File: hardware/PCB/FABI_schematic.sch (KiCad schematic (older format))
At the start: 40 parts, among them J1 Cliff_68125, J10 Conn_01x03_Male, J11 dispaly_connector_91601-304LF, J2 Cliff_68125, J3 Cliff_68125, J4 Cliff_68125, J5 Cliff_68125, J6 Cliff_68125, J7 Cliff_68125, J8 Cliff_68125, J9 Conn_02x05_Odd_Even, U1 MPXV7007GP, U2 ProMicro

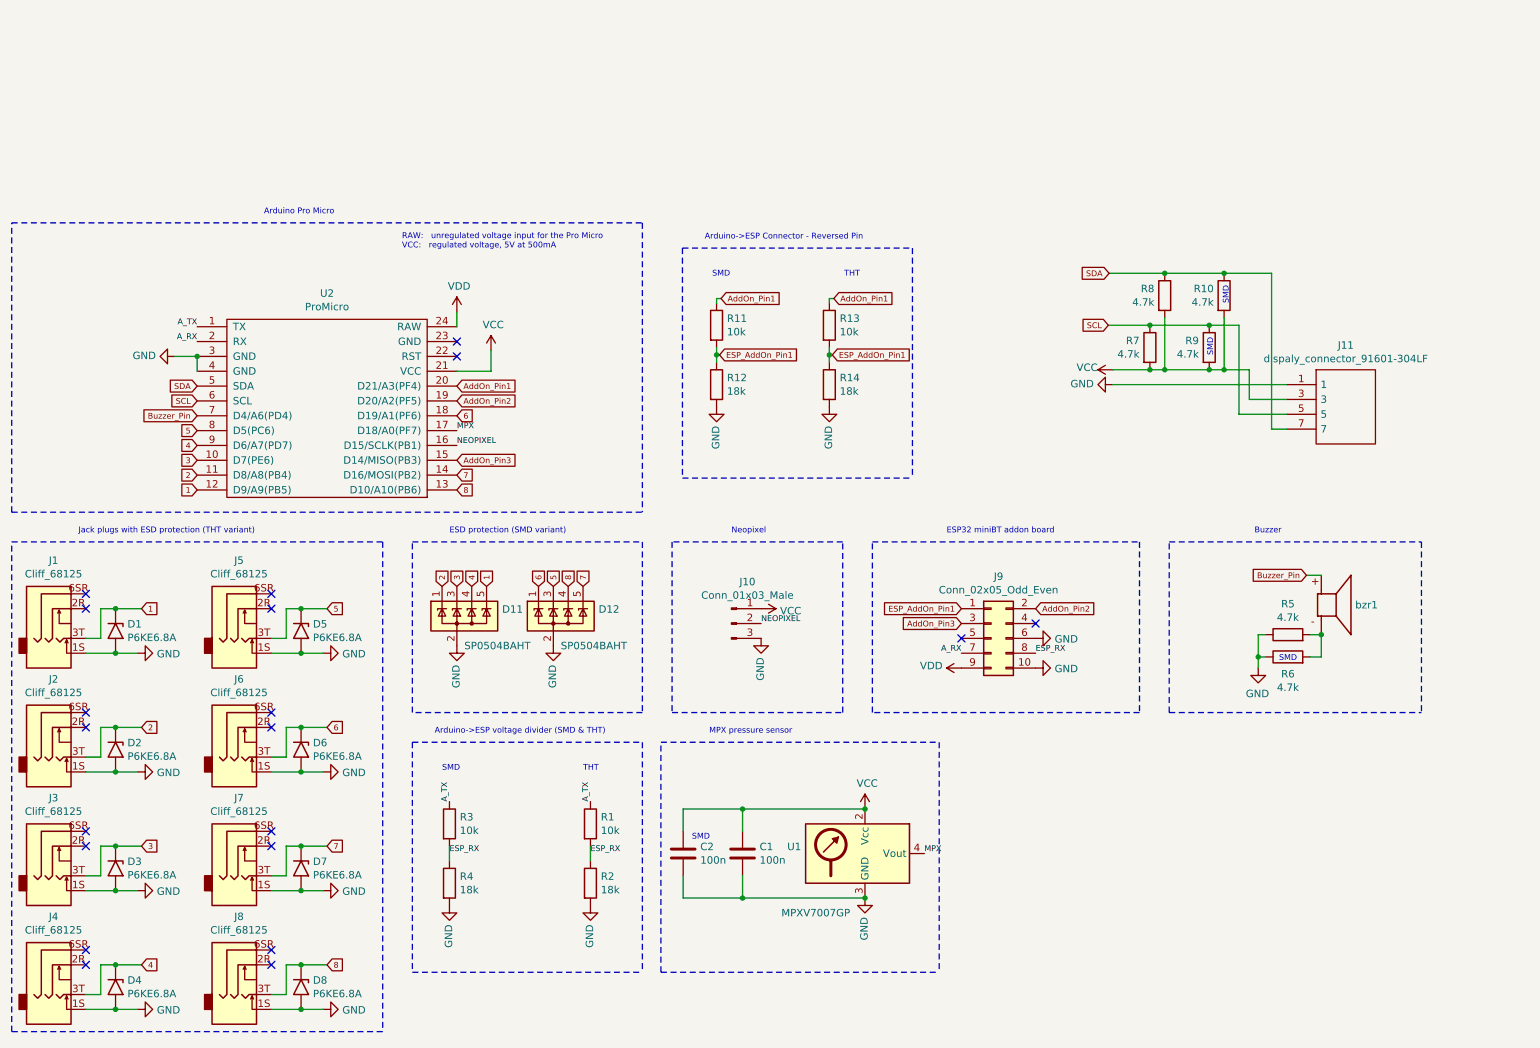
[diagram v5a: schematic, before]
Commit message: PCB v2, after Feedback (according to Meeting 2)
Signed-off-by: fussthalerandreas <fussthaler.andreas1997@gmail.com>
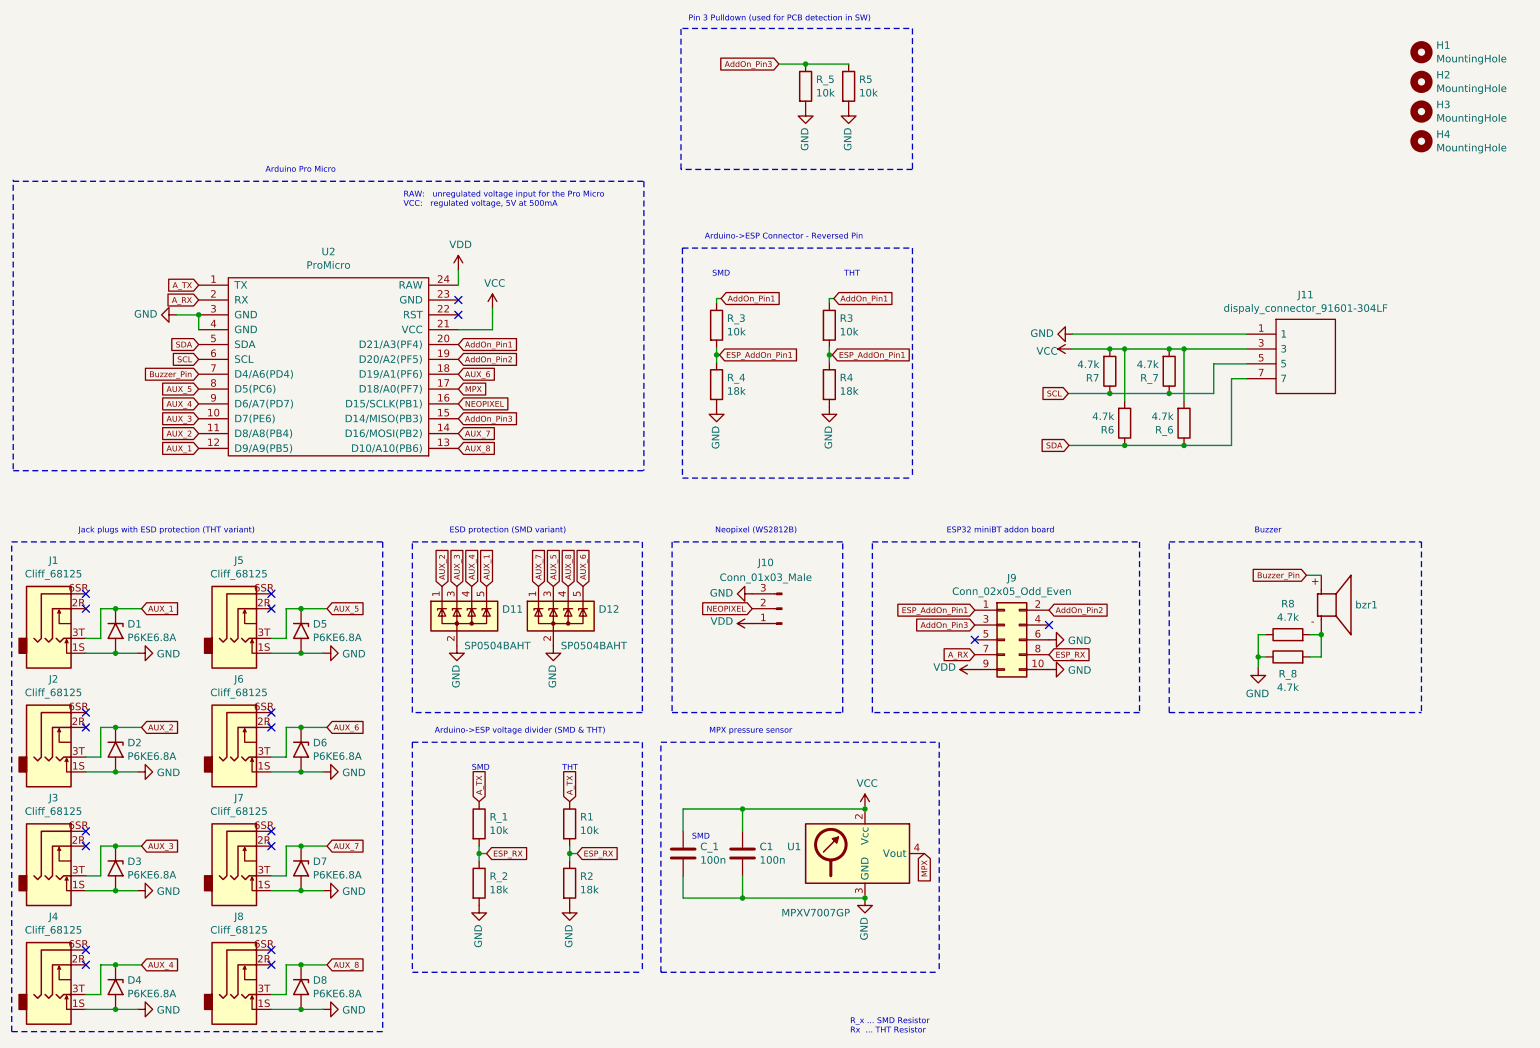
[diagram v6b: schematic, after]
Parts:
- added H1, H2, H3, H4: MountingHole, MountingHole:MountingHole_3mm, symbol Mechanical:MountingHole
- added R5: 10k, Resistor_THT:R_Axial_DIN0204_L3.6mm_D1.6mm_P7.62mm_Horizontal, symbol Device:R
- added R_5: 10k, Resistor_SMD:R_0805_2012Metric_Pad1.20x1.40mm_HandSolder, symbol Device:R
- renumbered C2 to C_1, R13 to R3, R14 to R4, R8 to R6, R5 to R8, R3 to R_1, R4 to R_2, R11 to R_3, R12 to R_4, R10 to R_6, R9 to R_7, R6 to R_8
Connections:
- net AddOn_Pin3: now also R5.1, R_5.1
- net GND: now also R5.2, R_5.2
- net VCC: no longer J10.1 (Pin_1)
- net VDD: now also J10.1 (Pin_1)
- net 1 renamed AUX_1
- net 2 renamed AUX_2
- net 3 renamed AUX_3
- net 4 renamed AUX_4
- net 5 renamed AUX_5
- net 6 renamed AUX_6
- net AUX_6: now also D12.5 (K); no longer D12.1 (K)
- net 7 renamed AUX_7
- net AUX_7: now also D12.1 (K); no longer D12.5 (K)
- net 8 renamed AUX_8
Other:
- note added: "Neopixel (WS2812B)"
- note added: "Pin 3 Pulldown (used for PCB detection in SW)"
- note added: "R_x ... SMD Resistor\nRx ... THT Resistor\n"
- note removed: "Neopixel"
- moved on the sheet: J10, J11, J9, R1, R2, R6, R7, R_1, R_2, R_6, R_7, U2

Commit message: adapted PCB according to Feedback (mounting holes, ProMicro pins enlarged, TVS-diods and arrays repositioned and routes enlarged to 0.5mm, NeoPixel SMD Pads, +element labels)
Signed-off-by: fussthalerandreas <fussthaler.andreas1997@gmail.com>
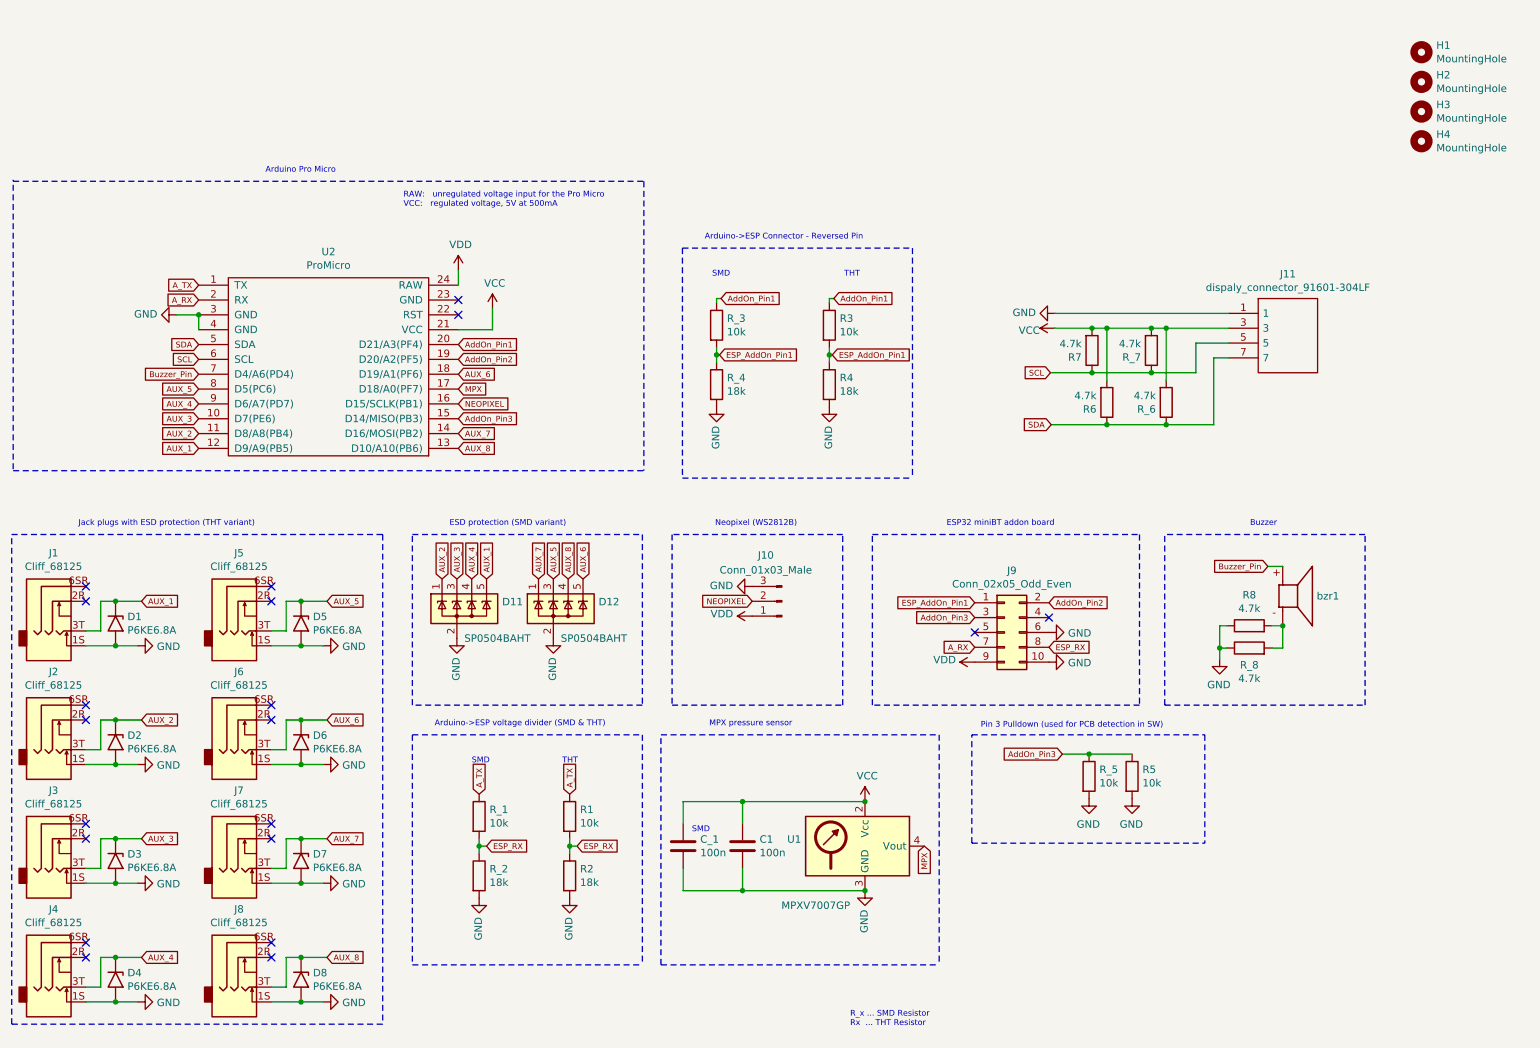
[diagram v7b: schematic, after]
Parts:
- U2: footprint ProMicro:ProMicro -> FABI_customLibs:ProMicro
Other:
- moved on the sheet: C1, C_1, D1, D11, D12, D2, D3, D4, D5, D6, D7, D8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
